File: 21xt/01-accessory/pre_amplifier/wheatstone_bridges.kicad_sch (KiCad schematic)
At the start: 0 parts

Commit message: completed schemtic
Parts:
- added R21, R23, R25, R27, R29, R31, R33, R35, R37, R39, R41, R43, R45, R47, R49, R51, R53, R55, R57, R59, R61, R63, R65, R67, R69, R71, R73, R75, R77, R79: 330, symbol Device:R
- added R22, R24, R26, R28, R30, R32, R34, R36, R38, R40, R42, R44, R46, R48, R50, R52, R54, R56, R58, R60, R62, R64, R66, R68, R70, R72, R74, R76, R78, R80: 20, symbol Device:R
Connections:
- new net: R37.2, R38.1
- new net: R53.2, R54.1
- new net: R47.2, R48.1
- new net: R73.2, R74.1
- new net: R21.2, R22.1
- new net: R25.2, R26.1
- new net: R59.2, R60.1
- new net: R35.2, R36.1
- new net: R79.2, R80.1
- new net: R41.2, R42.1
- new net: R45.2, R46.1
- new net: R55.2, R56.1
- new net: R57.2, R58.1
- new net: R27.2, R28.1
- new net: R39.2, R40.1
- new net: R67.2, R68.1
- new net: R69.2, R70.1
- new net: R75.2, R76.1
- new net: R63.2, R64.1
- new net: R61.2, R62.1
- new net: R29.2, R30.1
- new net: R23.2, R24.1
- new net: R33.2, R34.1
- new net: R65.2, R66.1
- new net: R51.2, R52.1
- new net: R77.2, R78.1
- new net: R71.2, R72.1
- new net: R31.2, R32.1
- new net: R49.2, R50.1
- new net: R43.2, R44.1
- new net 5v_reful: R21.1, R27.1, R33.1, R39.1, R45.1, R51.1, R57.1, R63.1, R69.1, R75.1
- new net GND: R24.2, R26.2, R30.2, R32.2, R36.2, R38.2, R42.2, R44.2, R48.2, R50.2, R54.2, R56.2, R60.2, R62.2, R66.2, R68.2, R72.2, R74.2, R78.2, R80.2
- new net Switch_x1: R22.2, R23.1
- new net Switch_x11: R52.2, R53.1
- new net Switch_x13: R58.2, R59.1
- new net Switch_x15: R64.2, R65.1
- new net Switch_x17: R70.2, R71.1
- new net Switch_x19: R76.2, R77.1
- new net Switch_x3: R28.2, R29.1
- new net Switch_x5: R34.2, R35.1
- new net Switch_x7: R40.2, R41.1
- new net Switch_x9: R46.2, R47.1
- new net Switch_y10: R49.1
- new net Switch_y12: R55.1
- new net Switch_y14: R61.1
- new net Switch_y16: R67.1
- new net Switch_y18: R73.1
- new net Switch_y2: R25.1
- new net Switch_y20: R79.1
- new net Switch_y4: R31.1
- new net Switch_y6: R37.1
- new net Switch_y8: R43.1
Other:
- note added: "3 wire connection"
- note added: "Strain gauges: 1) refulator 2) switches for strain gauges 3) 'strain gauge input' connector"

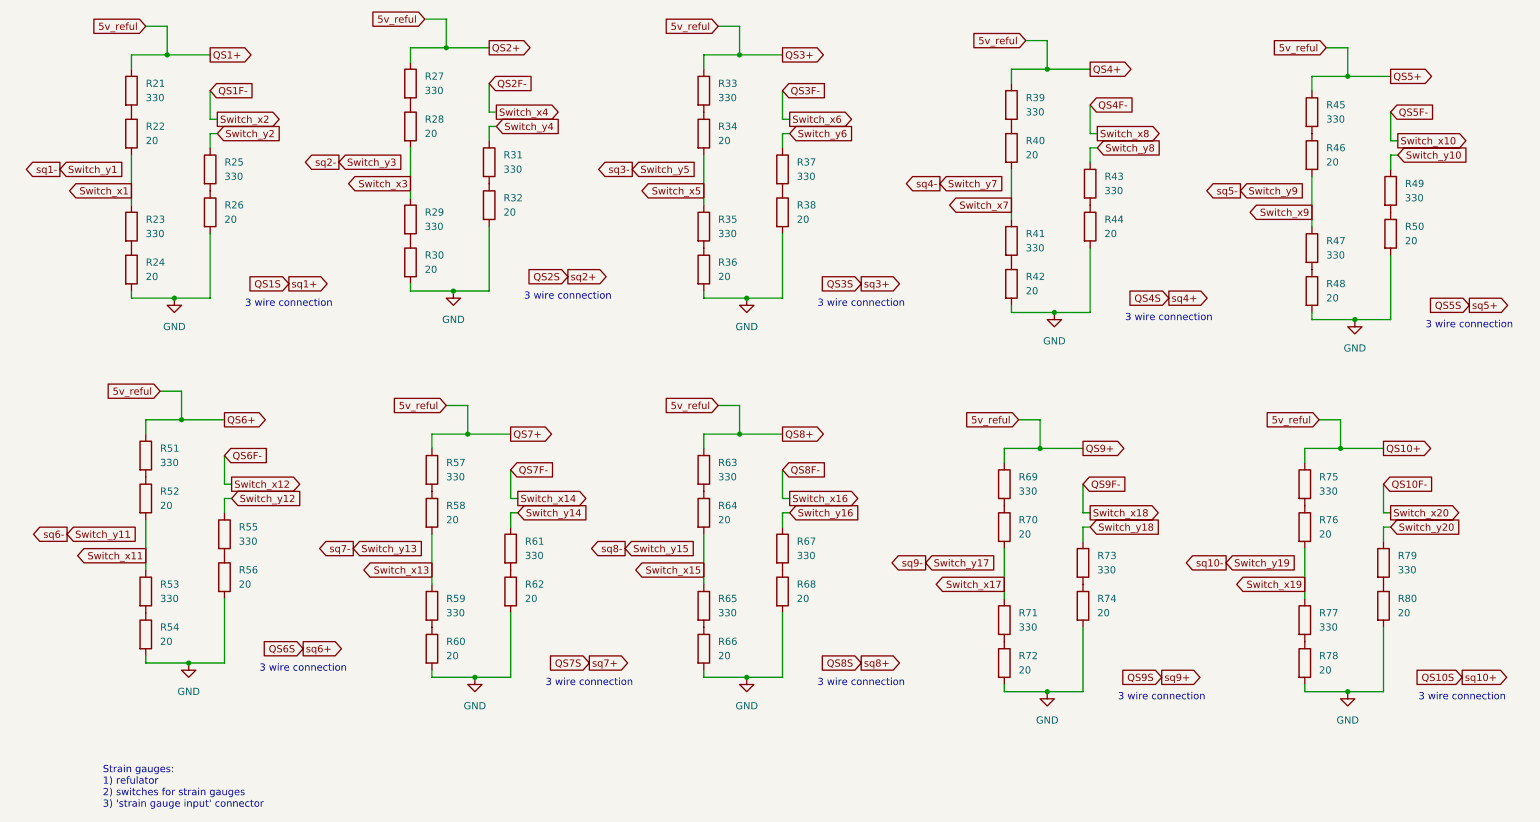
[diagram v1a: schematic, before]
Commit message: Reviewed schematic
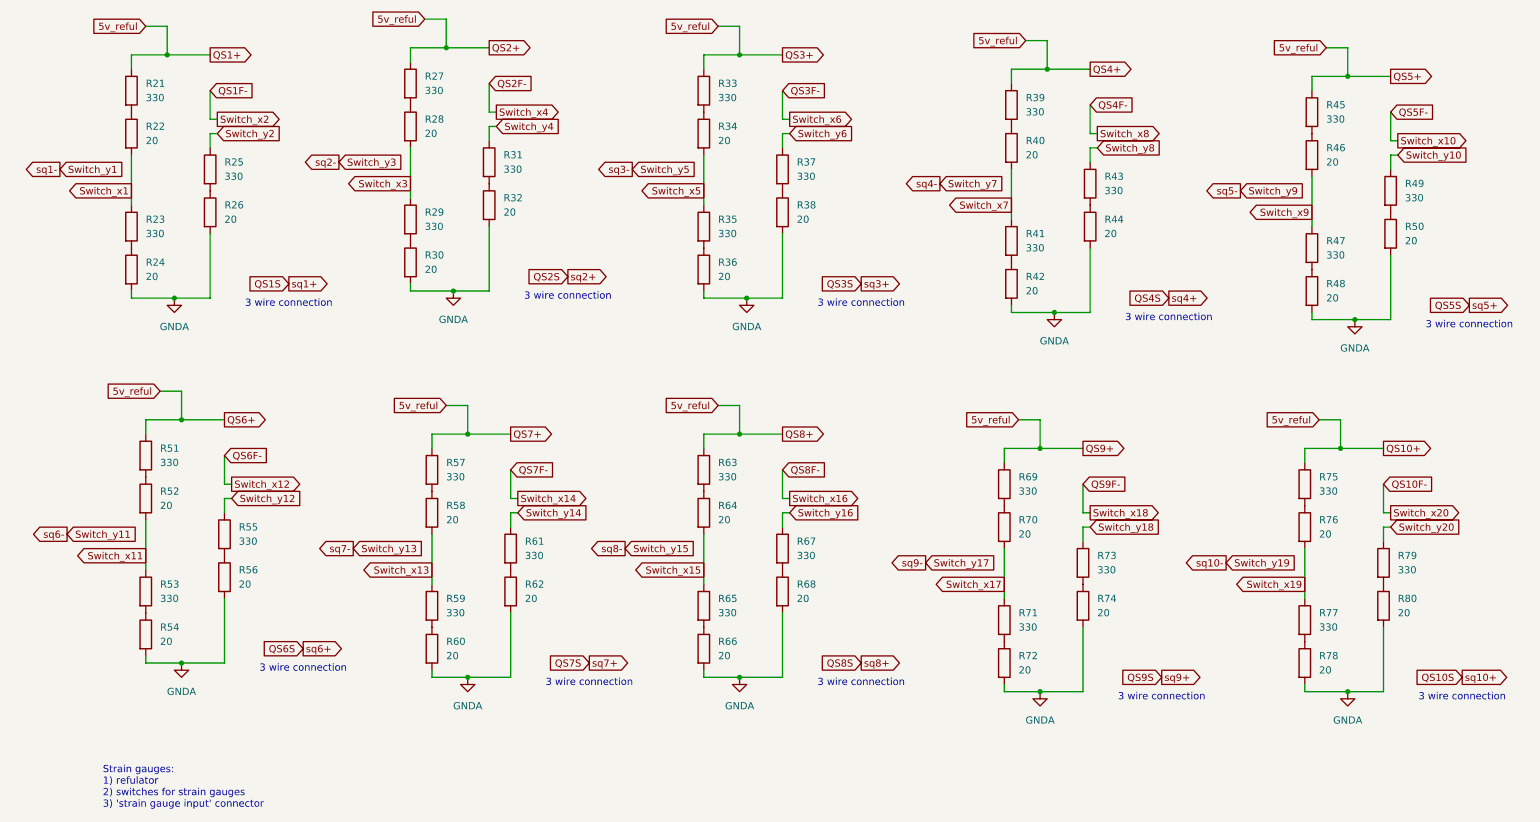
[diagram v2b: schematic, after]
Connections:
- net GND renamed GNDA

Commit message: assigned footprints
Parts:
- R21, R22, R23, R24, R25, R26, R27, R28, R29, R30, R31, R32, R33, R34, R35, R36, R37, R38, R39, R40, R41, R42, R43, R44, R45, R46, R47, R48, R49, R50, R51, R52, R53, R54, R55, R56, R57, R58, R59, R60, R61, R62, R63, R64, R65, R66, R67, R68, R69, R70, R71, R72, R73, R74, R75, R76, R77, R78, R79, R80: footprint (none) -> Resistor_SMD:R_0402_1005Metric
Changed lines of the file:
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@@
 			)
 		)
-		(property "Footprint" ""
+		(property "Footprint" "Resistor_SMD:R_0402_1005Metric"
 			(at 149.352 52.07 90)
 			(effects
@@
 			)
 		)
-		(property "Footprint" ""
+		(property "Footprint" "Resistor_SMD:R_0402_1005Metric"
 			(at 36.322 134.62 90)
 			(effects
@@
 			)
 		)
-		(property "Footprint" ""
+		(property "Footprint" "Resistor_SMD:R_0402_1005Metric"
 			(at 243.332 66.04 90)
 			(effects
@@
 			)
 		)
-		(property "Footprint" ""
+		(property "Footprint" "Resistor_SMD:R_0402_1005Metric"
 			(at 202.692 129.54 90)
 			(effects
@@
 			)
 		)
-		(property "Footprint" ""
+		(property "Footprint" "Resistor_SMD:R_0402_1005Metric"
 			(at 33.782 45.72 90)
 			(effects
@@
 			)
 		)
-		(property "Footprint" ""
+		(property "Footprint" "Resistor_SMD:R_0402_1005Metric"
 			(at 47.752 59.69 90)
 			(effects
@@
 			)
 		)
-		(property "Footprint" ""
+		(property "Footprint" "Resistor_SMD:R_0402_1005Metric"
 			(at 87.122 129.54 90)
 			(effects
@@
 			)
 		)
-		(property "Footprint" ""
+		(property "Footprint" "Resistor_SMD:R_0402_1005Metric"
 			(at 33.782 38.1 90)
 			(effects
@@
 			)
 		)
-		(property "Footprint" ""
+		(property "Footprint" "Resistor_SMD:R_0402_1005Metric"
 			(at 135.382 62.23 90)
 			(effects
@@
 			)
 		)
-		(property "Footprint" ""
+		(property "Footprint" "Resistor_SMD:R_0402_1005Metric"
 			(at 243.332 73.66 90)
 			(effects
@@
 			)
 		)
-		(property "Footprint" ""
+		(property "Footprint" "Resistor_SMD:R_0402_1005Metric"
 			(at 256.032 129.54 90)
 			(effects
@@
 			)
 		)
-		(property "Footprint" ""
+		(property "Footprint" "Resistor_SMD:R_0402_1005Metric"
 			(at 189.992 72.39 90)
 			(effects
@@
 			)
 		)
-		(property "Footprint" ""
+		(property "Footprint" "Resistor_SMD:R_0402_1005Metric"
 			(at 243.332 49.53 90)
 			(effects
@@
 			)
 		)
-		(property "Footprint" ""
+		(property "Footprint" "Resistor_SMD:R_0402_1005Metric"
 			(at 50.292 124.46 90)
 			(effects
@@
 			)
 		)
-		(property "Footprint" ""
+		(property "Footprint" "Resistor_SMD:R_0402_1005Metric"
 			(at 87.122 105.41 90)
 			(effects
@@
 			)
 		)
-		(property "Footprint" ""
+		(property "Footprint" "Resistor_SMD:R_0402_1005Metric"
 			(at 83.312 44.45 90)
 			(effects
@@
 			)
 		)
-		(property "Footprint" ""
+		(property "Footprint" "Resistor_SMD:R_0402_1005Metric"
 			(at 189.992 40.64 90)
 			(effects
@@
 			)
 		)
-		(property "Footprint" ""
+		(property "Footprint" "Resistor_SMD:R_0402_1005Metric"
 			(at 149.352 127 90)
 			(effects
@@
 			)
 		)
-		(property "Footprint" ""
+		(property "Footprint" "Resistor_SMD:R_0402_1005Metric"
 			(at 188.722 107.95 90)
 			(effects
@@
 			)
 		)
-		(property "Footprint" ""
+		(property "Footprint" "Resistor_SMD:R_0402_1005Metric"
 			(at 242.062 115.57 90)
 			(effects
@@
 			)
 		)
-		(property "Footprint" ""
+		(property "Footprint" "Resistor_SMD:R_0402_1005Metric"
 			(at 135.382 69.85 90)
 			(effects
@@
 			)
 		)
-		(property "Footprint" ""
+		(property "Footprint" "Resistor_SMD:R_0402_1005Metric"
 			(at 47.752 52.07 90)
 			(effects
@@
 			)
 		)
-		(property "Footprint" ""
+		(property "Footprint" "Resistor_SMD:R_0402_1005Metric"
 			(at 135.382 113.03 90)
 			(effects
@@
 			)
 		)
-		(property "Footprint" ""
+		(property "Footprint" "Resistor_SMD:R_0402_1005Metric"
 			(at 101.092 127 90)
 			(effects
@@
 			)
 		)
-		(property "Footprint" ""
+		(property "Footprint" "Resistor_SMD:R_0402_1005Metric"
 			(at 202.692 121.92 90)
 			(effects
@@
 			)
 		)
-		(property "Footprint" ""
+		(property "Footprint" "Resistor_SMD:R_0402_1005Metric"
 			(at 83.312 68.58 90)
 			(effects
@@
 			)
 		)
-		(property "Footprint" ""
+		(property "Footprint" "Resistor_SMD:R_0402_1005Metric"
 			(at 33.782 62.23 90)
 			(effects
@@
 			)
 		)
-		(property "Footprint" ""
+		(property "Footprint" "Resistor_SMD:R_0402_1005Metric"
 			(at 189.992 48.26 90)
 			(effects
@@
 			)
 		)
-		(property "Footprint" ""
+		(property "Footprint" "Resistor_SMD:R_0402_1005Metric"
 			(at 135.382 45.72 90)
 			(effects
@@
 			)
 		)
-		(property "Footprint" ""
+		(property "Footprint" "Resistor_SMD:R_0402_1005Metric"
 			(at 242.062 107.95 90)
 			(effects
@@
 			)
 		)
-		(property "Footprint" ""
+		(property "Footprint" "Resistor_SMD:R_0402_1005Metric"
 			(at 149.352 59.69 90)
 			(effects
@@
 			)
 		)
-		(property "Footprint" ""
+		(property "Footprint" "Resistor_SMD:R_0402_1005Metric"
 			(at 135.382 137.16 90)
 			(effects
@@
 			)
 		)
-		(property "Footprint" ""
+		(property "Footprint" "Resistor_SMD:R_0402_1005Metric"
 			(at 36.322 102.87 90)
 			(effects
@@
 			)
 		)
-		(property "Footprint" ""
+		(property "Footprint" "Resistor_SMD:R_0402_1005Metric"
 			(at 242.062 132.08 90)
 			(effects
@@
 			)
 		)
-		(property "Footprint" ""
+		(property "Footprint" "Resistor_SMD:R_0402_1005Metric"
 			(at 188.722 115.57 90)
 			(effects
@@
 			)
 		)
-		(property "Footprint" ""
+		(property "Footprint" "Resistor_SMD:R_0402_1005Metric"
 			(at 83.312 36.83 90)
 			(effects
@@
 			)
 		)
-		(property "Footprint" ""
+		(property "Footprint" "Resistor_SMD:R_0402_1005Metric"
 			(at 243.332 41.91 90)
 			(effects
@@
 			)
 		)
-		(property "Footprint" ""
+		(property "Footprint" "Resistor_SMD:R_0402_1005Metric"
 			(at 188.722 139.7 90)
 			(effects
@@
 			)
 		)
-		(property "Footprint" ""
+		(property "Footprint" "Resistor_SMD:R_0402_1005Metric"
 			(at 188.722 132.08 90)
 			(effects
@@
 			)
 		)
-		(property "Footprint" ""
+		(property "Footprint" "Resistor_SMD:R_0402_1005Metric"
 			(at 135.382 38.1 90)
 			(effects
@@
 			)
 		)
-		(property "Footprint" ""
+		(property "Footprint" "Resistor_SMD:R_0402_1005Metric"
 			(at 36.322 110.49 90)
 			(effects
@@
 			)
 		)
-		(property "Footprint" ""
+		(property "Footprint" "Resistor_SMD:R_0402_1005Metric"
 			(at 189.992 64.77 90)
 			(effects
@@
 			)
 		)
-		(property "Footprint" ""
+		(property "Footprint" "Resistor_SMD:R_0402_1005Metric"
 			(at 50.292 116.84 90)
 			(effects
@@
 			)
 		)
-		(property "Footprint" ""
+		(property "Footprint" "Resistor_SMD:R_0402_1005Metric"
 			(at 135.382 105.41 90)
 			(effects
@@
 			)
 		)
-		(property "Footprint" ""
+		(property "Footprint" "Resistor_SMD:R_0402_1005Metric"
 			(at 97.282 50.8 90)
 			(effects
@@
 			)
 		)
-		(property "Footprint" ""
+		(property "Footprint" "Resistor_SMD:R_0402_1005Metric"
 			(at 87.122 137.16 90)
 			(effects
@@
 			)
 		)
-		(property "Footprint" ""
+		(property "Footprint" "Resistor_SMD:R_0402_1005Metric"
 			(at 257.302 63.5 90)
 			(effects
@@
 			)
 		)
-		(property "Footprint" ""
+		(property "Footprint" "Resistor_SMD:R_0402_1005Metric"
 			(at 203.962 54.61 90)
 			(effects
@@
 			)
 		)
-		(property "Footprint" ""
+		(property "Footprint" "Resistor_SMD:R_0402_1005Metric"
 			(at 203.962 62.23 90)
 			(effects
@@
 			)
 		)
-		(property "Footprint" ""
+		(property "Footprint" "Resistor_SMD:R_0402_1005Metric"
 			(at 149.352 119.38 90)
 			(effects
@@
 			)
 		)
-		(property "Footprint" ""
+		(property "Footprint" "Resistor_SMD:R_0402_1005Metric"
 			(at 242.062 139.7 90)
 			(effects
@@
 			)
 		)
-		(property "Footprint" ""
+		(property "Footprint" "Resistor_SMD:R_0402_1005Metric"
 			(at 257.302 55.88 90)
 			(effects
@@
 			)
 		)
-		(property "Footprint" ""
+		(property "Footprint" "Resistor_SMD:R_0402_1005Metric"
 			(at 33.782 69.85 90)
 			(effects
@@
 			)
 		)
-		(property "Footprint" ""
+		(property "Footprint" "Resistor_SMD:R_0402_1005Metric"
 			(at 101.092 119.38 90)
 			(effects
@@
 			)
 		)
-		(property "Footprint" ""
+		(property "Footprint" "Resistor_SMD:R_0402_1005Metric"
 			(at 83.312 60.96 90)
 			(effects
@@
 			)
 		)
-		(property "Footprint" ""
+		(property "Footprint" "Resistor_SMD:R_0402_1005Metric"
 			(at 36.322 127 90)
 			(effects
@@
 			)
 		)
-		(property "Footprint" ""
+		(property "Footprint" "Resistor_SMD:R_0402_1005Metric"
 			(at 135.382 129.54 90)
 			(effects
@@
 			)
 		)
-		(property "Footprint" ""
+		(property "Footprint" "Resistor_SMD:R_0402_1005Metric"
 			(at 256.032 121.92 90)
 			(effects
@@
 			)
 		)
-		(property "Footprint" ""
+		(property "Footprint" "Resistor_SMD:R_0402_1005Metric"
 			(at 97.282 58.42 90)
 			(effects
@@
 			)
 		)
-		(property "Footprint" ""
+		(property "Footprint" "Resistor_SMD:R_0402_1005Metric"
 			(at 87.122 113.03 90)
 			(effects
